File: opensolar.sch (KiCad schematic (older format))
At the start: 60 parts

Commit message: sense resistor
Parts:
- removed C? (x6): C, symbol C
- added C? (x2): 22pf, symbol C
- added C?: 100nf, symbol C
- added C?: 10uf, symbol C
- added C? (x4): 1uf, symbol C
- added C?: .1uf, symbol C
- added C? (x30): C, symbol C
- added C? (x2): 10nf, symbol C
- added D? (x5): D_Schottky, symbol D_Schottky
- added P?: USB_OTG, symbol USB_OTG
- added P?: microSD, symbol CONN_01X10
- added P?: Panel+, symbol CONN_01X01
- added P?: Panel-, symbol CONN_01X01
- added P?: Batt-, symbol CONN_01X01
- added P?: Batt+, symbol CONN_01X01
- added Q? (x2): S8050, TO-92, symbol S8050
- added R? (x2): 470, symbol R
- added R? (x6): 10k, symbol R
- added R? (x2): 0.0005ohm, symbol R
- added R? (x2): 499, symbol R
- added R?: 0, symbol R
- added R? (x2): R, symbol R
- added W?: TP_RX, symbol TEST_1P
- added W?: TP_TX, symbol TEST_1P
- added W?: TP_SDA, symbol TEST_1P
- added W?: TP_SCL, symbol TEST_1P
- added W?: TP_340, symbol TEST_1P
- added W?: TP_RST, symbol TEST_1P
- added Y?: 12mhz, symbol Crystal_Small
- R?: value 10k -> 0
- R? (x2): value 10k -> 2k
- R? (x2): value R -> 499
- R? (x2): value R -> 10
- R? (x2): value R -> 4.99
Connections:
- net +3V3: now also R?.2, R?.2, U?.4 (V3), P?.4 (P4), R?.1, R?.1, R?.2
- net +5V: now also U?.17 (VDD), C?.1, D?.1 (K); no longer R?.2, R?.2, R?.2
- net 10V: now also U?.21 (VCCB), U?.25 (VCCA), C?.2, C?.2
- net GND: now also U?.1 (GND), C?.1, C?.1, C?.1, C?.1, C?.1, C?.2, C?.2, C?.2, C?.2, C?.2, C?.2, C?.2, C?.2, C?.2, C?.2, C?.2, C?.2, C?.2, C?.2, C?.2, C?.2, C?.2, C?.2, C?.2, C?.2, C?.2, C?.2, C?.2, C?.2, C?.2, C?.2, C?.2, C?.2, C?.2, C?.2, C?.2, C?.2, P?.1 (P1), P?.1 (P1), P?.5 (GND), P?.6 (P6), P?.6 (shield), R?.1, R?.2, R?.2
- net SCL: now also U?.14 (GPIO5), W?.1
- net SDA: now also U?.13 (GPIO4), W?.1
- net SIB: now also Q?.1 (D), C?.1, C?.1, C?.1, C?.1, C?.1, C?.1, C?.1, C?.1, C?.1, C?.1, C?.1, C?.1, C?.1, C?.1, R?.2
- net VPP: now also C?.2, P?.1 (P1), R?.1, R?.2; no longer C?.2, R?.2, U?.8 (VIN)
- net nRST: now reaches U?.1 (REST)
- net nRST: now also Q?.3 (C)
- net RST: now reaches U?.10 (GPIO15)
- net RST: now also R?.2, R?.1
- net CS_SD: now reaches U?.11 (GPIO2)
- net CS_SD: now also P?.2 (P2), R?.1
- net GPIO0: now reaches R?.1, U?.12 (GPIO0)
- net GPIO0: now also Q?.3 (C), R?.2
- net RXD: now reaches U?.15 (RXD)
- net RXD: now also R?.2, W?.1
- net TXD: now reaches U?.16 (TXD)
- net TXD: now also R?.2, W?.1
- net SCLK: now reaches U?.5 (GPIO14)
- net SCLK: now also P?.5 (P5)
- net MISO: now reaches U?.6 (GPIO12)
- net MISO: now also P?.7 (P7)
- net MOSI: now reaches U?.7 (GPIO13)
- net MOSI: now also P?.3 (P3)
- net at R?.1, U?.1 (RST): now also W?.1
- net AVOUT: now reaches U?.17 (AVOUT)
- net AVOUT: now also C?.1, R?.1, R?.2
- net SIA: now reaches U?.1 (SIA)
- net SIA: now also R?.2
- net at R?.1, U?.13 (SOB): now also C?.2
- net LB: now reaches U?.18 (HSB)
- net LB: now also L?.2, Q?.1 (D), Q?.3 (S), C?.1
- net Q2: now reaches U?.19 (HOB)
- net Q2: now also R?.1, D?.1 (K)
- net SOA: now reaches U?.2 (SOA)
- net SOA: now also C?.1, R?.2
- net at U?.20 (HBB): now also C?.2
- net Q4: now reaches U?.22 (LOB)
- net Q4: now also R?.1, D?.1 (K)
- net Q3: now reaches U?.24 (LOA)
- net Q3: now also R?.2, D?.1 (K)
- net at U?.26 (HBA): now also C?.2
- net Q1: now reaches U?.27 (HOA)
- net Q1: now also R?.2, D?.1 (K)
- net LA: now reaches U?.28 (HSA)
- net LA: now also L?.1, Q?.1 (D), Q?.3 (S), C?.1
- net at Q?.1 (D): now also C?.1, C?.1, C?.1, C?.1, C?.1, C?.1, C?.1, C?.1, C?.1, C?.1, C?.1, C?.1, C?.1, C?.1, C?.1, R?.1, R?.1
- net at Q?.2 (G), R?.1: now also D?.2 (A)
- net at Q?.2 (G), R?.1: now also D?.2 (A), R?.2
- net at Q?.2 (G), R?.2: now also D?.2 (A) (x2)
- net at U?.13 (DTR): now also Q?.1 (E), R?.1
- net at U?.14 (RTS): now also Q?.1 (E), R?.1
- net at U?.16 (VCC): now also C?.2, C?.2, R?.2, W?.1
- net at U?.2 (TXD): now also R?.1
- net at U?.3 (RXD): now also R?.1
- net at U?.5 (UD+): now also P?.3 (D+)
- net at U?.6 (UD-): now also P?.2 (D-)
- net at U?.7 (XI): now also C?.1, Y?.1
- net at U?.8 (XO): now also C?.1, Y?.2
- net SOB renamed +48V
- net +48V: now also C?.2, R?.2, U?.8 (VIN), C?.2, P?.1 (P1), R?.1, R?.1
- new net: D?.2 (A), P?.1 (VCC)
- new net: Q?.2 (B), R?.2 (x2)
- no-connect marks 0 -> 10
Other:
- note added: "100v input, 48 volt lead acid battery max\n60 amp limits\nMPPT charge controller with wifi management\n"
- note added: "sense resistor\nWSLF2512L5000FE\n0.5mOhm 6watt 1%\n$0.79@10\n$0.29@1000"
- moved on the sheet: C?, D?, L?, Q?, R?, SW?, U?

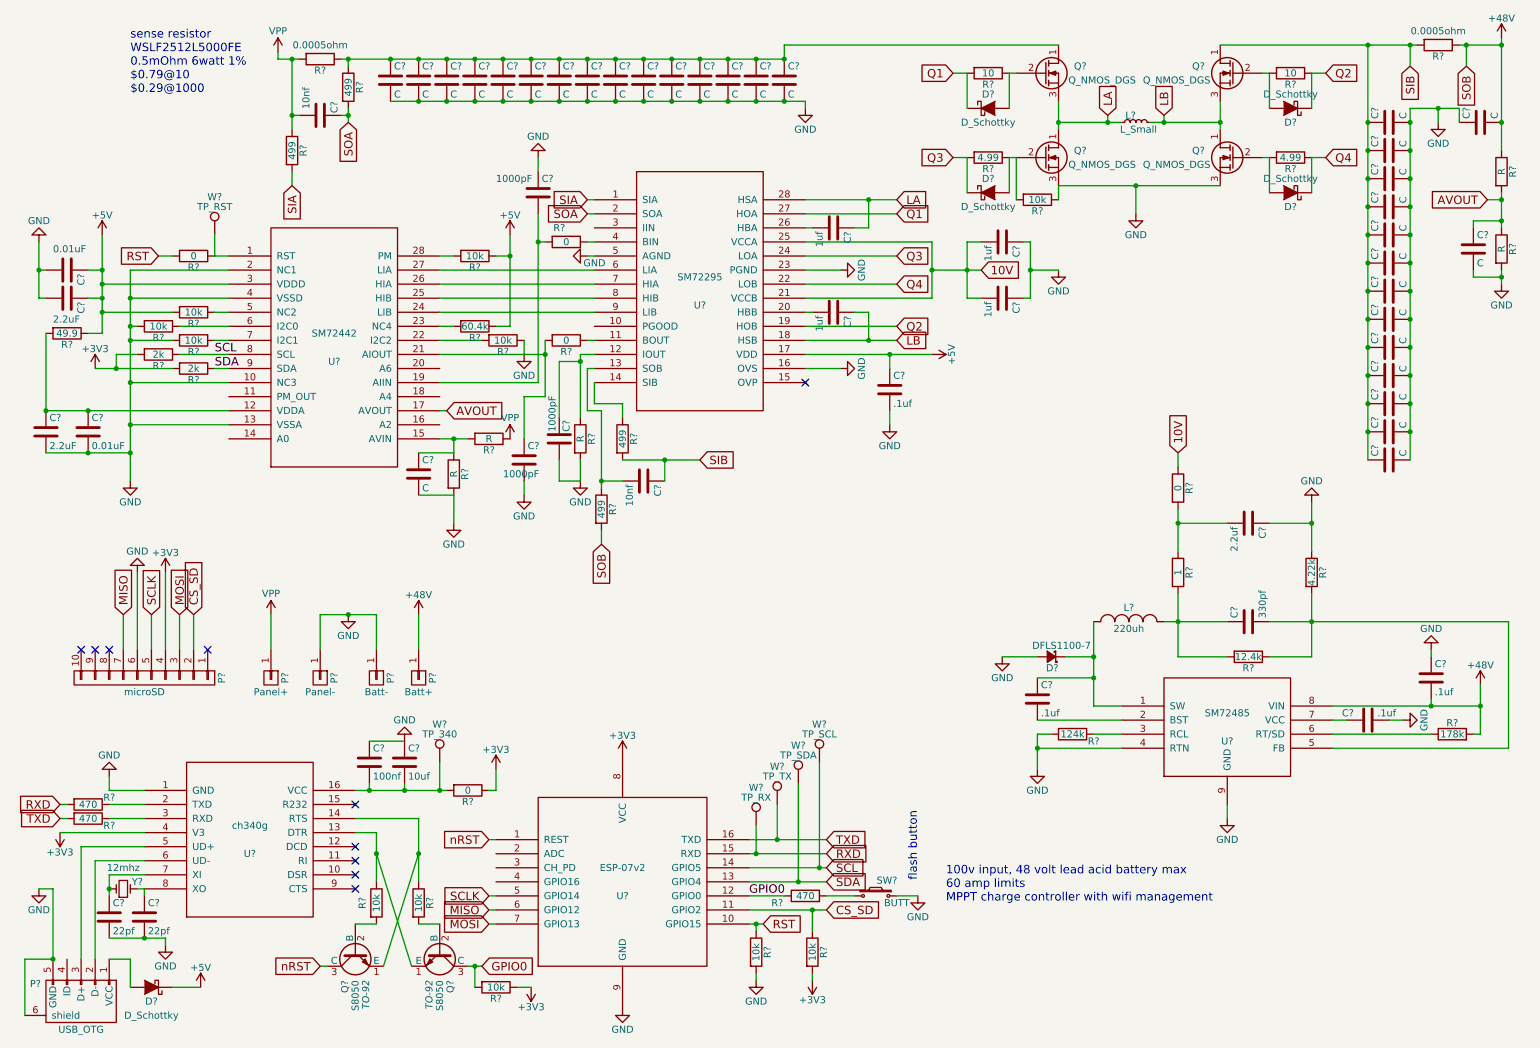
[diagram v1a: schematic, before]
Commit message: update CH340g input
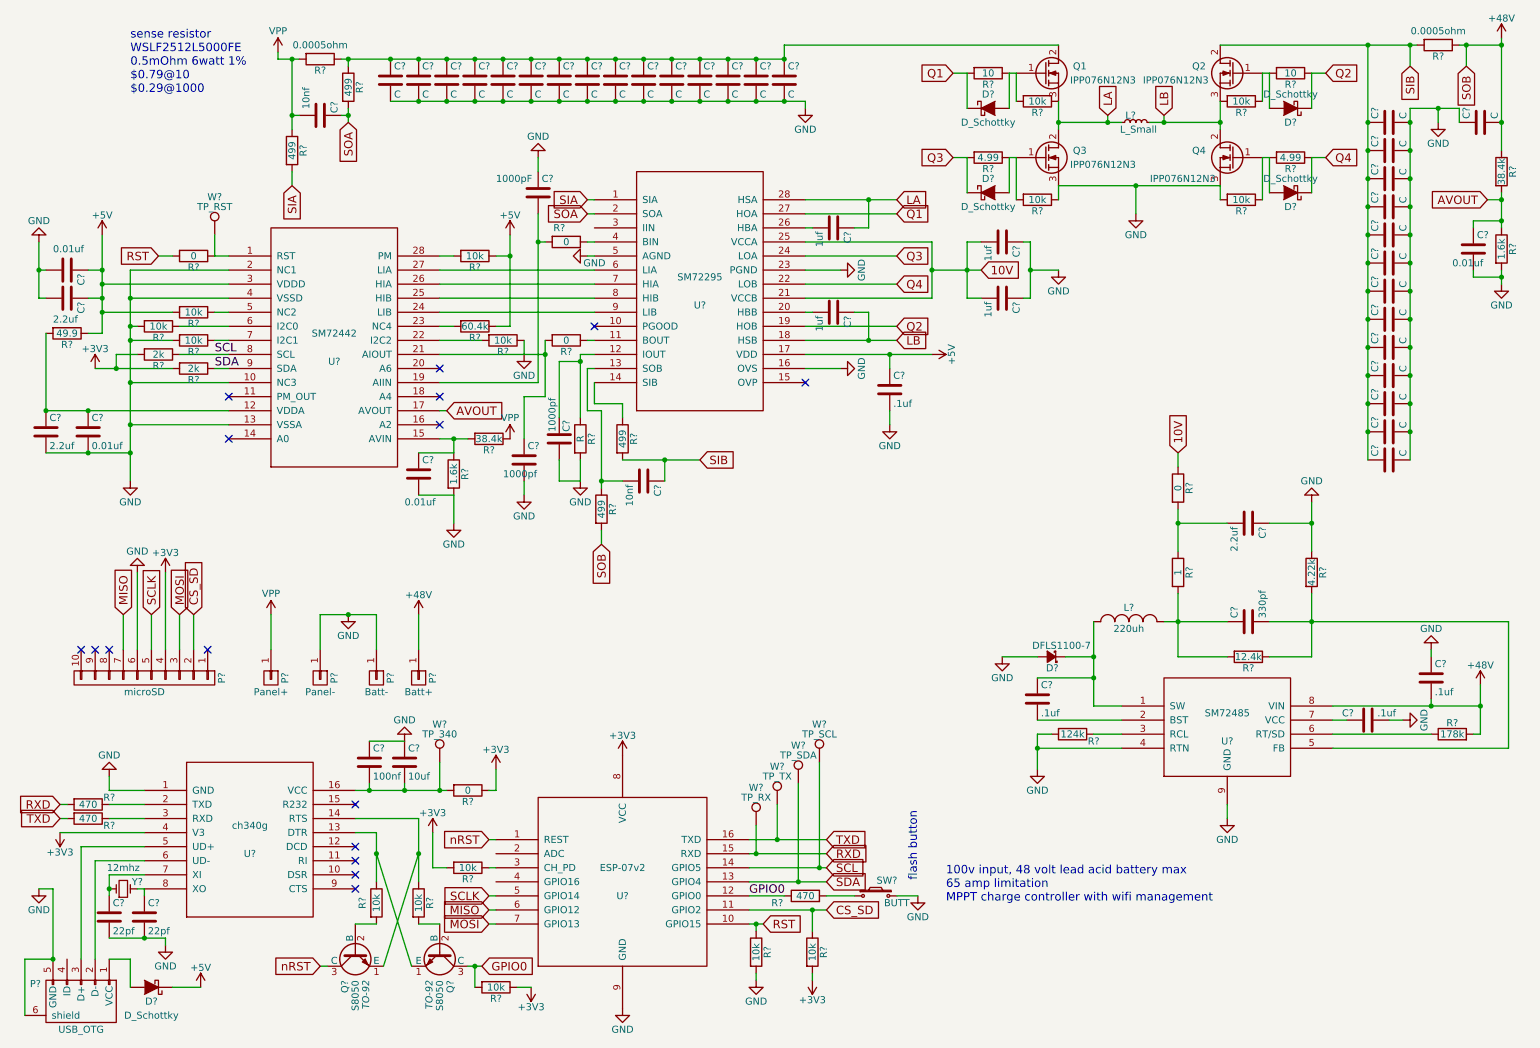
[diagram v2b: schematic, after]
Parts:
- removed Q? (x4): Q_NMOS_DGS, symbol Q_NMOS_DGS
- added Q1, Q2, Q3, Q4: IPP076N12N3, symbol Q_NMOS_GDS
- added R? (x4): 10k, symbol R
- C? (x2): value 0.01uF -> 0.01uf
- C? (x2): value 2.2uF -> 2.2uf
- C? (x2): value C -> 0.01uf
- C? (x2): value 1000pF -> 1000pf
- R? (x2): value R -> 38.4k
- R? (x2): value R -> 1.6k
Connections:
- net +3V3: now also R?.2
- net GND: now also Q3.3 (S), Q4.3 (S), R?.2
- net LA: now also Q1.3 (S), Q3.2 (D), R?.1
- net LB: now also Q2.3 (S), Q4.2 (D), R?.2
- net SIB: now also Q2.2 (D)
- net at U?.3 (CH_PD): now also R?.1
- net at C?.1, C?.1, C?.1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: now also Q1.2 (D)
- net at D?.2 (A), R?.1: now also Q1.1 (G), R?.2
- net at D?.2 (A), R?.1, R?.2: now also Q3.1 (G)
- net at D?.2 (A), R?.2: now also Q2.1 (G), R?.1
- net at D?.2 (A), R?.2: now also Q4.1 (G), R?.1
- no-connect marks 10 -> 16
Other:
- note added: "100v input, 48 volt lead acid battery max\n65 amp limitation\nMPPT charge controller with wifi management\n"
- note removed: "100v input, 48 volt lead acid battery max\n60 amp limits\nMPPT charge controller with wifi management\n"
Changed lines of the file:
@@
 P 800 2350
 F 0 "C?" H 825 2450 50  0000 L CNN
-F 1 "0.01uF" V 650 2250 50  0000 L CNN
+F 1 "0.01uf" V 650 2250 50  0000 L CNN
 F 2 "" H 838 2200 50  0000 C CNN
 F 3 "" H 800 2350 50  0000 C CNN
@@
 P 800 2550
 F 0 "C?" H 825 2650 50  0000 L CNN
-F 1 "2.2uF" V 950 2450 50  0000 L CNN
+F 1 "2.2uf" V 950 2450 50  0000 L CNN
 F 2 "" H 838 2400 50  0000 C CNN
 F 3 "" H 800 2550 50  0000 C CNN
@@
 P 650 3500
 F 0 "C?" H 675 3600 50  0000 L CNN
-F 1 "2.2uF" H 675 3400 50  0000 L CNN
+F 1 "2.2uf" H 675 3400 50  0000 L CNN
 F 2 "" H 688 3350 50  0000 C CNN
 F 3 "" H 650 3500 50  0000 C CNN
@@
 P 950 3500
 F 0 "C?" H 975 3600 50  0000 L CNN
-F 1 "0.01uF" H 975 3400 50  0000 L CNN
+F 1 "0.01uf" H 975 3400 50  0000 L CNN
 F 2 "" H 988 3350 50  0000 C CNN
 F 3 "" H 950 3500 50  0000 C CNN
@@
 P 3800 3550
 F 0 "R?" V 3880 3550 50  0000 C CNN
-F 1 "R" V 3800 3550 50  0000 C CNN
+F 1 "38.4k" V 3800 3550 50  0000 C CNN
 F 2 "" V 3730 3550 50  0000 C CNN
 F 3 "" H 3800 3550 50  0000 C CNN
@@
 P 3550 3800
 F 0 "R?" V 3630 3800 50  0000 C CNN
-F 1 "R" V 3550 3800 50  0000 C CNN
+F 1 "1.6k" V 3550 3800 50  0000 C CNN
 F 2 "" V 3480 3800 50  0000 C CNN
 F 3 "" H 3550 3800 50  0000 C CNN
@@
 P 3300 3800
 F 0 "C?" H 3325 3900 50  0000 L CNN
-F 1 "C" H 3325 3700 50  0000 L CNN
+F 1 "0.01uf" H 3200 3600 50  0000 L CNN
 F 2 "" H 3338 3650 50  0000 C CNN
 F 3 "" H 3300 3800 50  0000 C CNN
@@
 P 4050 3700
 F 0 "C?" H 4075 3800 50  0000 L CNN
-F 1 "1000pF" H 3900 3600 50  0000 L CNN
+F 1 "1000pf" H 3900 3600 50  0000 L CNN
 F 2 "" H 4088 3550 50  0000 C CNN
 F 3 "" H 4050 3700 50  0000 C CNN
@@
 $EndComp
 $Comp
-L Q_NMOS_DGS Q?
-U 1 1 5886D2A4
-P 7750 950
-F 0 "Q?" H 8050 1000 50  0000 R CNN
-F 1 "Q_NMOS_DGS" H 8400 900 50  0000 R CNN
-F 2 "" H 7950 1050 50  0000 C CNN
-F 3 "" H 7750 950 50  0000 C CNN
-	1    7750 950
-	1    0    0    -1
-$EndComp
-$Comp
-L Q_NMOS_DGS Q?
-U 1 1 5886D2FF
-P 7750 1550
-F 0 "Q?" H 8050 1600 50  0000 R CNN
-F 1 "Q_NMOS_DGS" H 8400 1500 50  0000 R CNN
-F 2 "" H 7950 1650 50  0000 C CNN
-F 3 "" H 7750 1550 50  0000 C CNN
-	1    7750 1550
-	1    0    0    -1
-$EndComp
-$Comp
-L Q_NMOS_DGS Q?
-U 1 1 5886D7E6
-P 9100 950
-F 0 "Q?" H 9400 1000 50  0000 R CNN
-F 1 "Q_NMOS_DGS" H 9750 900 50  0000 R CNN
-F 2 "" H 9300 1050 50  0000 C CNN
-F 3 "" H 9100 950 50  0000 C CNN
-	1    9100 950
-	-1   0    0    -1
-$EndComp
-$Comp
-L Q_NMOS_DGS Q?
-U 1 1 5886D89B
-P 9100 1550
-F 0 "Q?" H 9400 1600 50  0000 R CNN
-F 1 "Q_NMOS_DGS" H 9750 1500 50  0000 R CNN
-F 2 "" H 9300 1650 50  0000 C CNN
-F 3 "" H 9100 1550 50  0000 C CNN
-	1    9100 1550
-	-1   0    0    -1
-$EndComp
-$Comp
 L R R?
 U 1 1 5886DC1C
@@
 P 4300 3550
 F 0 "C?" V 4350 3600 50  0000 L CNN
-F 1 "1000pF" V 4250 3600 50  0000 L CNN
+F 1 "1000pf" V 4250 3600 50  0000 L CNN
 F 2 "" H 4338 3400 50  0000 C CNN
 F 3 "" H 4300 3550 50  0000 C CNN
@@
 Connection ~ 5900 1150
 Text Notes 7050 6850 0    60   ~ 0
-100v input, 48 volt lead acid battery max\n60 amp limits\nMPPT charge controller with wifi management\n
+100v input, 48 volt lead acid battery max\n65 amp limitation\nMPPT charge controller with wifi management\n
 $Comp
 L SM72295 U?
@@
 Wire Wire Line
 	10700 1200 10700 1300
-Wire Wire Line
-	10550 1300 10550 1200
 Connection ~ 10550 1200
 $Comp
@@
 P 11000 1650
 F 0 "R?" V 11080 1650 50  0000 C CNN
-F 1 "R" V 11000 1650 50  0000 C CNN
+F 1 "38.4k" V 11000 1650 50  0000 C CNN
 F 2 "" V 10930 1650 50  0000 C CNN
 F 3 "" H 11000 1650 50  0000 C CNN
@@
 P 11000 2200
 F 0 "R?" V 11080 2200 50  0000 C CNN
-F 1 "R" V 11000 2200 50  0000 C CNN
+F 1 "1.6k" V 11000 2200 50  0000 C CNN
 F 2 "" V 10930 2200 50  0000 C CNN
 F 3 "" H 11000 2200 50  0000 C CNN
@@
 P 10800 2200
 F 0 "C?" H 10825 2300 50  0000 L CNN
-F 1 "C" H 10825 2100 50  0000 L CNN
+F 1 "0.01uf" H 10650 2100 50  0000 L CNN
 F 2 "" H 10838 2050 50  0000 C CNN
 F 3 "" H 10800 2200 50  0000 C CNN
@@
 Wire Wire Line
 	7550 1550 7550 1850
+NoConn ~ 3450 3050
+NoConn ~ 3450 3250
+NoConn ~ 3450 3450
+NoConn ~ 1950 3550
+NoConn ~ 1950 3250
+NoConn ~ 4550 2750
+$Comp
+L R R?
+U 1 1 58A04350
+P 7700 1150
+F 0 "R?" V 7780 1150 50  0000 C CNN
+F 1 "10k" V 7700 1150 50  0000 C CNN
+F 2 "" V 7630 1150 50  0000 C CNN
+F 3 "" H 7700 1150 50  0000 C CNN
+	1    7700 1150
+	0    1    1    0
+$EndComp
+Wire Wire Line
+	7550 950  7550 1150
+$Comp
+L R R?
+U 1 1 58A05EC3
+P 3650 6600
+F 0 "R?" V 3730 6600 50  0000 C CNN
+F 1 "10k" V 3650 6600 50  0000 C CNN
+F 2 "" V 3580 6600 50  0000 C CNN
+F 3 "" H 3650 6600 50  0000 C CNN
+	1    3650 6600
+	0    1    1    0
+$EndComp
+Wire Wire Line
+	3800 6600 3850 6600
+$Comp
+L +3V3 #PWR?
+U 1 1 58A0630D
+P 3400 6350
+F 0 "#PWR?" H 3400 6200 50  0001 C CNN
+F 1 "+3V3" H 3400 6490 50  0000 C CNN
+F 2 "" H 3400 6350 50  0000 C CNN
+F 3 "" H 3400 6350 50  0000 C CNN
+	1    3400 6350
+	1    0    0    -1
+$EndComp
+Wire Wire Line
+	3400 6350 3400 6600
+Wire Wire Line
+	3400 6600 3500 6600
+$Comp
+L R R?
+U 1 1 58A08346
+P 9150 1150
+F 0 "R?" V 9230 1150 50  0000 C CNN
+F 1 "10k" V 9150 1150 50  0000 C CNN
+F 2 "" V 9080 1150 50  0000 C CNN
+F 3 "" H 9150 1150 50  0000 C CNN
+	1    9150 1150
+	0    1    1    0
+$EndComp
+Wire Wire Line
+	9300 1150 9300 950
+$Comp
+L R R?
+U 1 1 58A08810
+P 9150 1850
+F 0 "R?" V 9230 1850 50  0000 C CNN
+F 1 "10k" V 9150 1850 50  0000 C CNN
+F 2 "" V 9080 1850 50  0000 C CNN
+F 3 "" H 9150 1850 50  0000 C CNN
+	1    9150 1850
+	0    1    1    0
+$EndComp
+Wire Wire Line
+	9000 1750 9000 1850
+Wire Wire Line
+	9300 1850 9300 1550
+$Comp
+L Q_NMOS_GDS Q3
+U 1 1 58A0E1BD
+P 7750 1550
+F 0 "Q3" H 8050 1600 50  0000 R CNN
+F 1 "IPP076N12N3" H 8400 1500 50  0000 R CNN
+F 2 "" H 7950 1650 50  0000 C CNN
+F 3 "" H 7750 1550 50  0000 C CNN
+	1    7750 1550
+	1    0    0    -1
+$EndComp
+$Comp
+L Q_NMOS_GDS Q1
+U 1 1 58A0E73B
+P 7750 950
+F 0 "Q1" H 8050 1000 50  0000 R CNN
+F 1 "IPP076N12N3" H 8400 900 50  0000 R CNN
+F 2 "" H 7950 1050 50  0000 C CNN
+F 3 "" H 7750 950 50  0000 C CNN
+	1    7750 950
+	1    0    0    -1
+$EndComp
+$Comp
+L Q_NMOS_GDS Q2
+U 1 1 58A0E8E5
+P 9100 950
+F 0 "Q2" H 9400 1000 50  0000 R CNN
+F 1 "IPP076N12N3" H 9750 900 50  0000 R CNN
+F 2 "" H 9300 1050 50  0000 C CNN
+F 3 "" H 9100 950 50  0000 C CNN
+	1    9100 950
+	-1   0    0    -1
+$EndComp
+$Comp
+L Q_NMOS_GDS Q4
+U 1 1 58A0EE44
+P 9100 1550
+F 0 "Q4" H 9400 1600 50  0000 R CNN
+F 1 "IPP076N12N3" H 9700 1400 50  0000 R CNN
+F 2 "" H 9300 1650 50  0000 C CNN
+F 3 "" H 9100 1550 50  0000 C CNN
+	1    9100 1550
+	-1   0    0    -1
+$EndComp
+Wire Wire Line
+	10550 1200 10550 1300
 $EndSCHEMATC
